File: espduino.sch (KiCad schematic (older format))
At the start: 14 parts, among them IC101 ATMEGA168-A, P101 CONN_01X12, P102 CONN_01X12, P103 FTDI, P104 CONN_01X02, SW101 SPST, X101 16Mhz

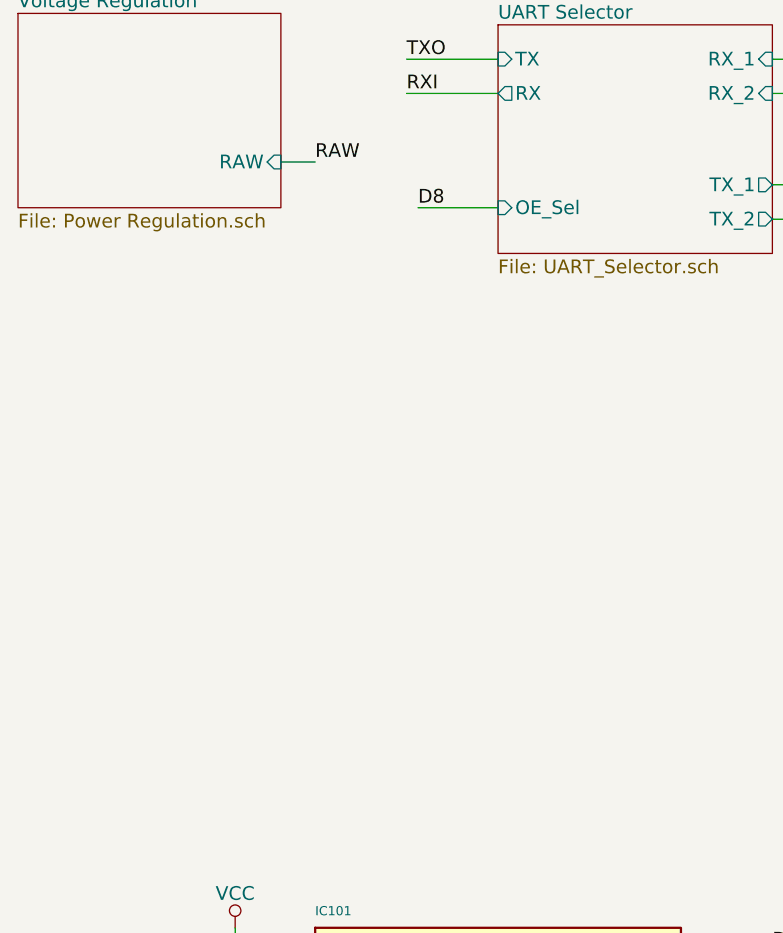
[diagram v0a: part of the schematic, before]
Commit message: Redesign the board and add USB
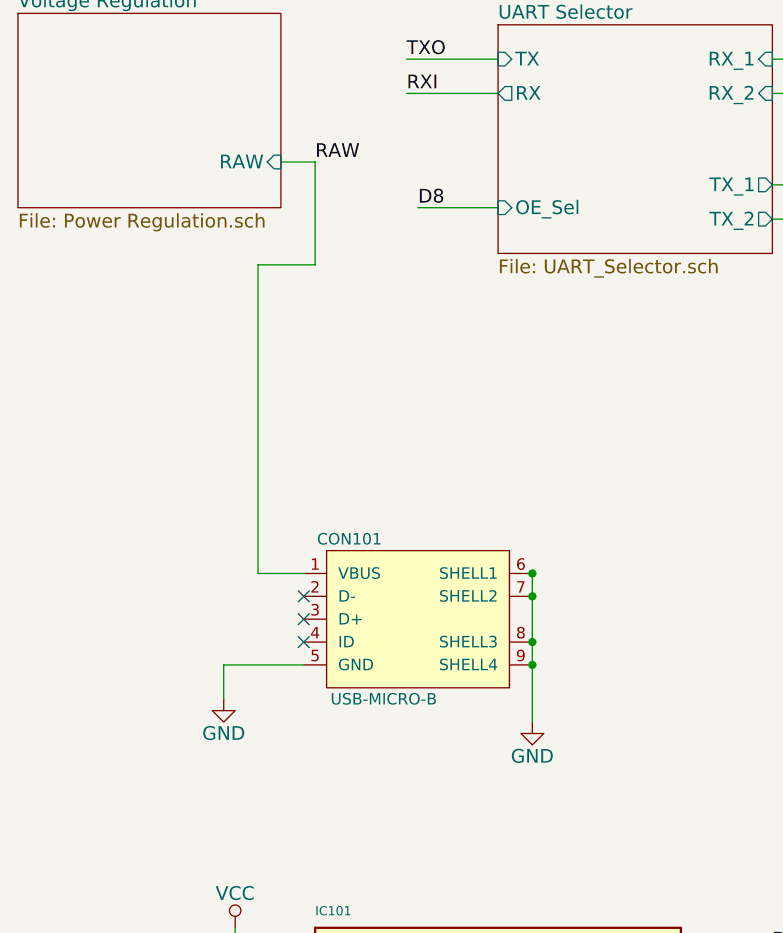
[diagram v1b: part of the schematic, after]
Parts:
- added CON101: USB-MICRO-B, symbol USB-MICRO-B
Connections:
- wire segments 91 -> 98
- no-connect marks 4 -> 7
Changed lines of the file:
@@
 Text Label 2300 850  0    60   ~ 0
 TXO
+$Comp
+L USB-MICRO-B CON101
+U 1 1 5538D1CF
+P 2350 3300
+F 0 "CON101" H 2050 3650 50  0000 C CNN
+F 1 "USB-MICRO-B" H 2200 2950 50  0000 C CNN
+F 2 "" H 2350 3200 50  0000 C CNN
+F 3 "" H 2350 3200 50  0000 C CNN
+	1    2350 3300
+	1    0    0    -1
+$EndComp
+Wire Wire Line
+	1850 3100 1650 3100
+Wire Wire Line
+	1650 3100 1650 1750
+Wire Wire Line
+	1650 1750 1900 1750
+Wire Wire Line
+	1900 1750 1900 1300
+$Comp
+L GND #PWR010
+U 1 1 5538D63B
+P 1500 3650
+F 0 "#PWR010" H 1500 3400 60  0001 C CNN
+F 1 "GND" H 1500 3500 60  0000 C CNN
+F 2 "" H 1500 3650 60  0000 C CNN
+F 3 "" H 1500 3650 60  0000 C CNN
+	1    1500 3650
+	1    0    0    -1
+$EndComp
+Wire Wire Line
+	1850 3500 1500 3500
+Wire Wire Line
+	1500 3500 1500 3650
+Wire Wire Line
+	2850 3100 2850 3750
+$Comp
+L GND #PWR011
+U 1 1 5538D7C0
+P 2850 3750
+F 0 "#PWR011" H 2850 3500 60  0001 C CNN
+F 1 "GND" H 2850 3600 60  0000 C CNN
+F 2 "" H 2850 3750 60  0000 C CNN
+F 3 "" H 2850 3750 60  0000 C CNN
+	1    2850 3750
+	1    0    0    -1
+$EndComp
+Connection ~ 2850 3500
+NoConn ~ 1850 3200
+NoConn ~ 1850 3300
+NoConn ~ 1850 3400
+Connection ~ 2850 3400
+Connection ~ 2850 3200
+Connection ~ 2850 3100
 $EndSCHEMATC

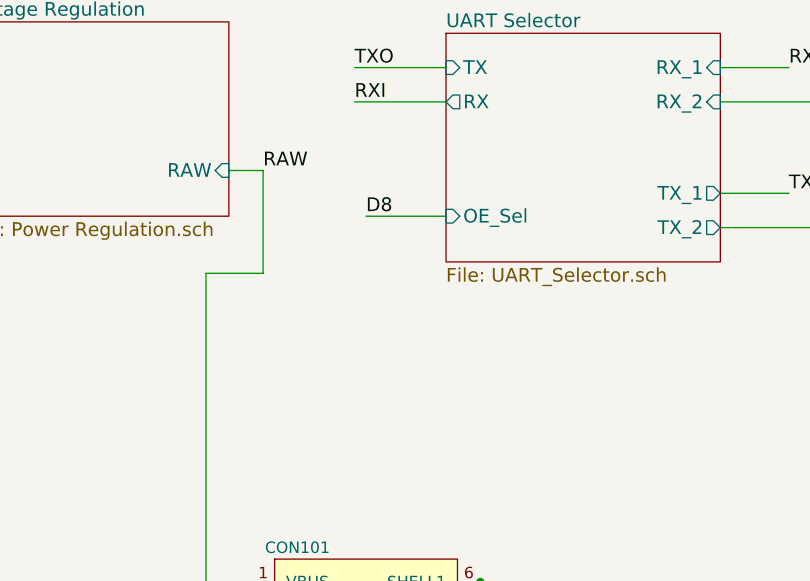
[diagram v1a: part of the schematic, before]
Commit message: Add mechanism to disable UART selector
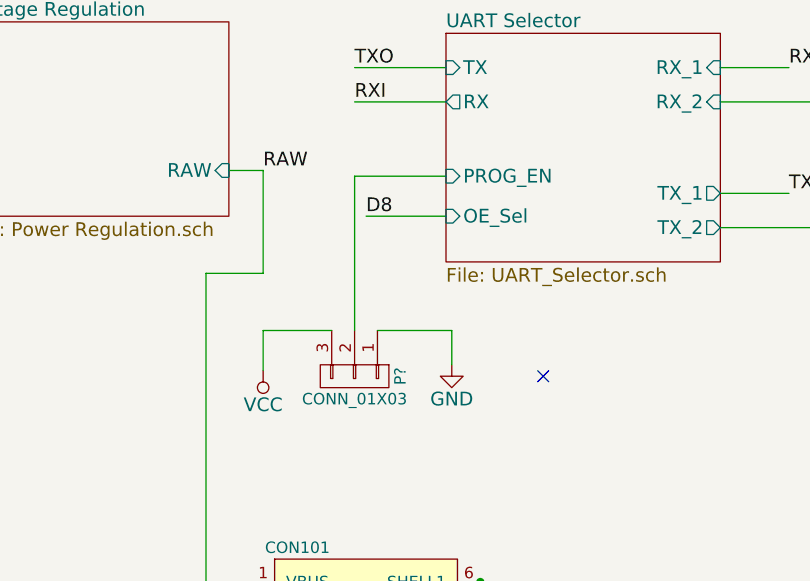
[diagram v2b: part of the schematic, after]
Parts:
- added P?: CONN_01X03, symbol CONN_01X03
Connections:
- wire segments 98 -> 104
- no-connect marks 7 -> 8
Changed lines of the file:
@@
 F7 "OE_Sel" I L 2700 1500 60
 F8 "RX" O L 2700 1000 60
+F9 "PROG_EN" I L 2700 1325 60
 $EndSheet
 Wire Wire Line
@@
 Connection ~ 2850 3200
 Connection ~ 2850 3100
+NoConn ~ 3125 2200
+Wire Wire Line
+	2300 1325 2700 1325
+$Comp
+L CONN_01X03 P?
+U 1 1 559105BB
+P 2300 2200
+F 0 "P?" H 2300 2400 50  0000 C CNN
+F 1 "CONN_01X03" V 2400 2200 50  0000 C CNN
+F 2 "" H 2300 2200 60  0000 C CNN
+F 3 "" H 2300 2200 60  0000 C CNN
+	1    2300 2200
+	0    1    1    0
+$EndComp
+Wire Wire Line
+	2300 2000 2300 1325
+$Comp
+L GND #PWR?
+U 1 1 559107D6
+P 2725 2150
+F 0 "#PWR?" H 2725 1900 60  0001 C CNN
+F 1 "GND" H 2725 2000 60  0000 C CNN
+F 2 "" H 2725 2150 60  0000 C CNN
+F 3 "" H 2725 2150 60  0000 C CNN
+	1    2725 2150
+	1    0    0    -1
+$EndComp
+$Comp
+L VCC #PWR?
+U 1 1 5591085F
+P 1900 2175
+F 0 "#PWR?" H 1900 2025 60  0001 C CNN
+F 1 "VCC" H 1900 2325 60  0000 C CNN
+F 2 "" H 1900 2175 60  0000 C CNN
+F 3 "" H 1900 2175 60  0000 C CNN
+	1    1900 2175
+	-1   0    0    1
+$EndComp
+Wire Wire Line
+	2725 2150 2725 2000
+Wire Wire Line
+	2725 2000 2400 2000
+Wire Wire Line
+	2200 2000 1900 2000
+Wire Wire Line
+	1900 2000 1900 2175
 $EndSCHEMATC

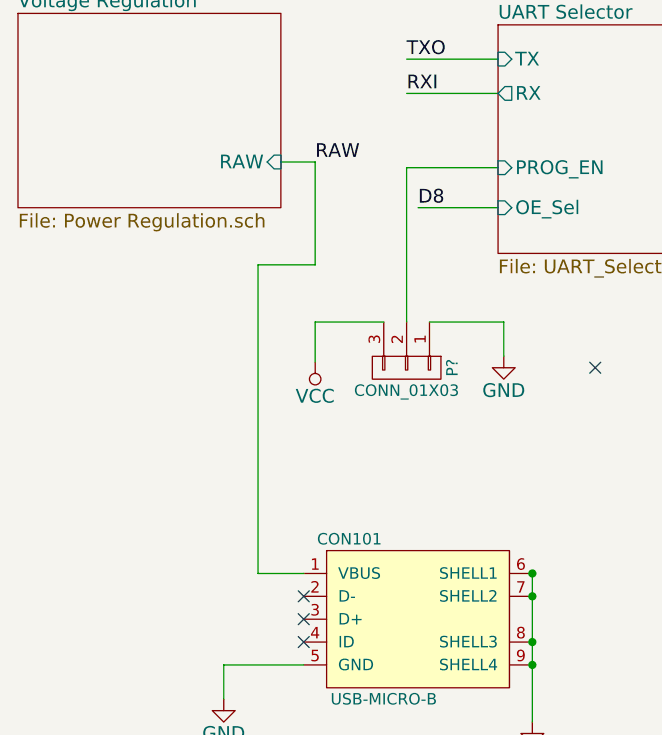
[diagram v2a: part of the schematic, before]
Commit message: Issue #4 RAW goes through LDO, +5v from USB doesn't
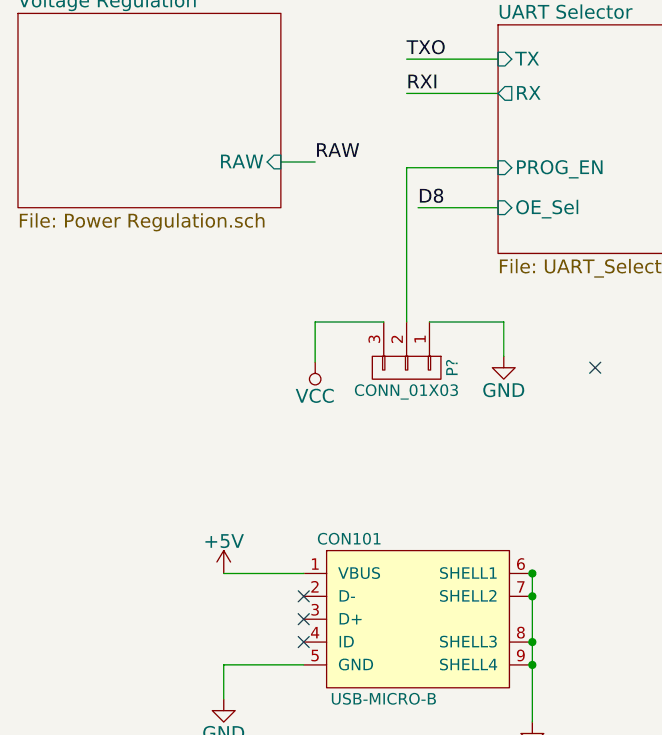
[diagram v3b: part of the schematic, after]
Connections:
- net labels added: +5V
- wire segments 104 -> 101
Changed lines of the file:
@@
 $EndComp
 Wire Wire Line
-	1850 3100 1650 3100
-Wire Wire Line
-	1650 3100 1650 1750
-Wire Wire Line
-	1650 1750 1900 1750
-Wire Wire Line
-	1900 1750 1900 1300
+	1500 3100 1850 3100
 $Comp
 L GND #PWR010
@@
 Wire Wire Line
 	1900 2000 1900 2175
+$Comp
+L +5V #PWR?
+U 1 1 55911357
+P 1500 3100
+F 0 "#PWR?" H 1500 2950 60  0001 C CNN
+F 1 "+5V" H 1500 3240 60  0000 C CNN
+F 2 "" H 1500 3100 60  0000 C CNN
+F 3 "" H 1500 3100 60  0000 C CNN
+	1    1500 3100
+	1    0    0    -1
+$EndComp
 $EndSCHEMATC

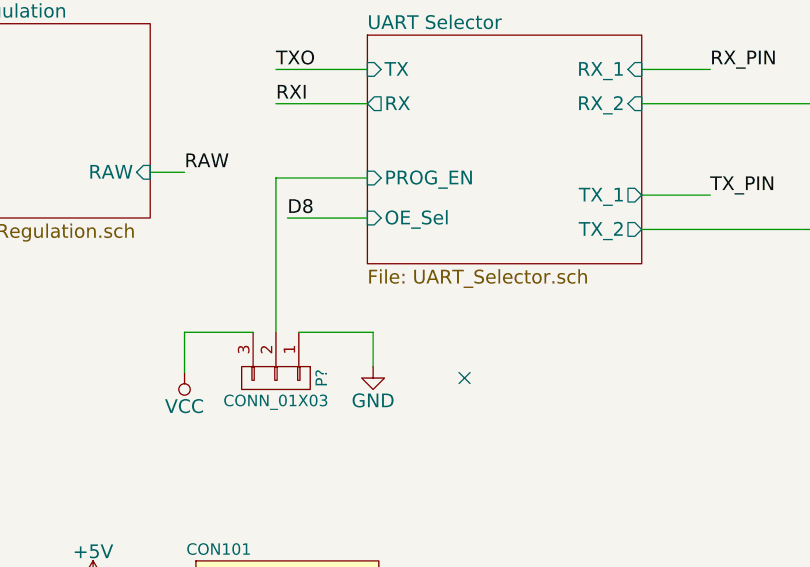
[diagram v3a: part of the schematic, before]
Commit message: Fix pin for ESP
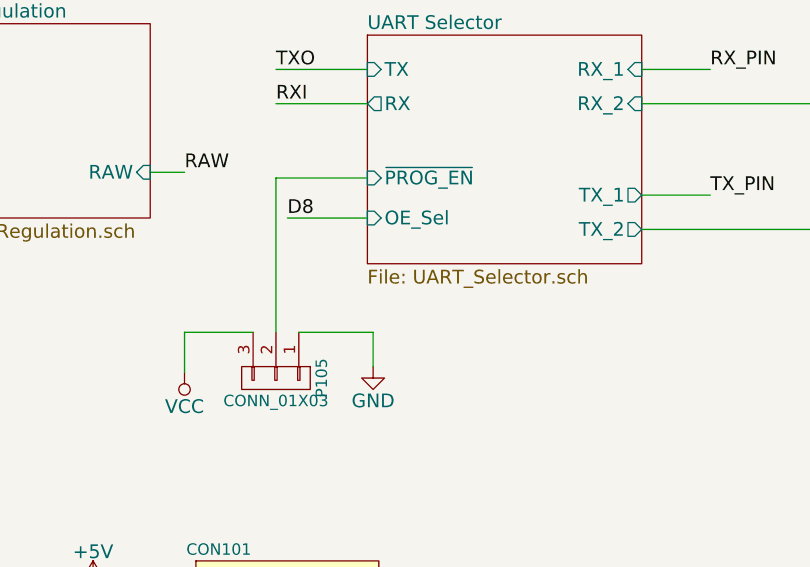
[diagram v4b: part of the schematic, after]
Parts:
- gave numbers to parts that had none: 1
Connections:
- no-connect marks 8 -> 7
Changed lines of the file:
@@
 F7 "OE_Sel" I L 2700 1500 60
 F8 "RX" O L 2700 1000 60
-F9 "PROG_EN" I L 2700 1325 60
+F9 "~PROG_EN" I L 2700 1325 60
 $EndSheet
 Wire Wire Line
@@
 Connection ~ 2850 3200
 Connection ~ 2850 3100
-NoConn ~ 3125 2200
 Wire Wire Line
 	2300 1325 2700 1325
 $Comp
-L CONN_01X03 P?
+L CONN_01X03 P105
 U 1 1 559105BB
 P 2300 2200
-F 0 "P?" H 2300 2400 50  0000 C CNN
+F 0 "P105" H 2300 2400 50  0000 C CNN
 F 1 "CONN_01X03" V 2400 2200 50  0000 C CNN
 F 2 "" H 2300 2200 60  0000 C CNN
@@
 	0    1    1    0
 $EndComp
-Wire Wire Line
-	2300 2000 2300 1325
 $Comp
-L GND #PWR?
+L GND #PWR012
 U 1 1 559107D6
 P 2725 2150
-F 0 "#PWR?" H 2725 1900 60  0001 C CNN
+F 0 "#PWR012" H 2725 1900 60  0001 C CNN
 F 1 "GND" H 2725 2000 60  0000 C CNN
 F 2 "" H 2725 2150 60  0000 C CNN
@@
 $EndComp
 $Comp
-L VCC #PWR?
+L VCC #PWR013
 U 1 1 5591085F
 P 1900 2175
-F 0 "#PWR?" H 1900 2025 60  0001 C CNN
+F 0 "#PWR013" H 1900 2025 60  0001 C CNN
 F 1 "VCC" H 1900 2325 60  0000 C CNN
 F 2 "" H 1900 2175 60  0000 C CNN
@@
 	1900 2000 1900 2175
 $Comp
-L +5V #PWR?
+L +5V #PWR014
 U 1 1 55911357
 P 1500 3100
-F 0 "#PWR?" H 1500 2950 60  0001 C CNN
+F 0 "#PWR014" H 1500 2950 60  0001 C CNN
 F 1 "+5V" H 1500 3240 60  0000 C CNN
 F 2 "" H 1500 3100 60  0000 C CNN
@@
 	1    0    0    -1
 $EndComp
+Wire Wire Line
+	2300 1325 2300 2000
 $EndSCHEMATC

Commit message: More fixes
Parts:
- removed IC101: ATMEGA168-A, LittlebushLogicFootPrints:TQFP32_08, symbol ATMEGA168-A
- added CON102: AVR-ISP-6, AVR-ISP-6, symbol AVR-ISP-6
- added IC101: ATMEGA328-P, TQFP32, symbol ATMEGA328-P
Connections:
- wire segments 101 -> 107
- no-connect marks 7 -> 8
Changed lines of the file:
@@
 $Descr A4 11693 8268
 encoding utf-8
-Sheet 1 4
+Sheet 1 5
 Title ""
 Date ""
@@
 $EndComp
 $Comp
-L VCC #PWR01
+L VCC #PWR104
 U 1 1 54F43D94
 P 1550 4650
-F 0 "#PWR01" H 1550 4500 60  0001 C CNN
+F 0 "#PWR104" H 1550 4500 60  0001 C CNN
 F 1 "VCC" H 1550 4800 60  0000 C CNN
 F 2 "" H 1550 4650 60  0000 C CNN
@@
 $EndComp
 $Comp
-L GND #PWR02
+L GND #PWR101
 U 1 1 54F43FD7
 P 1350 5750
-F 0 "#PWR02" H 1350 5500 60  0001 C CNN
+F 0 "#PWR101" H 1350 5500 60  0001 C CNN
 F 1 "GND" H 1350 5600 60  0000 C CNN
 F 2 "" H 1350 5750 60  0000 C CNN
@@
 $EndComp
 $Comp
-L GND #PWR03
+L GND #PWR105
 U 1 1 54F442ED
 P 1650 7050
-F 0 "#PWR03" H 1650 6800 60  0001 C CNN
+F 0 "#PWR105" H 1650 6800 60  0001 C CNN
 F 1 "GND" H 1650 6900 60  0000 C CNN
 F 2 "" H 1650 7050 60  0000 C CNN
@@
 Wire Wire Line
 	1550 5050 1750 5050
-Wire Wire Line
-	1750 4850 1550 4850
 Connection ~ 1550 4850
 Connection ~ 1550 4750
@@
 	1350 5350 1750 5350
 Wire Wire Line
-	1750 6850 1650 6850
-Wire Wire Line
-	1650 6850 1650 7050
-Wire Wire Line
 	1650 7050 1750 7050
 Wire Wire Line
 	1750 6950 1650 6950
-Connection ~ 1650 6950
 Wire Wire Line
 	3650 4750 3900 4750
@@
 Connection ~ 4700 5700
 $Comp
-L GND #PWR04
+L GND #PWR109
 U 1 1 54F456F6
 P 5350 5100
-F 0 "#PWR04" H 5350 4850 60  0001 C CNN
+F 0 "#PWR109" H 5350 4850 60  0001 C CNN
 F 1 "GND" H 5350 4950 60  0000 C CNN
 F 2 "" H 5350 5100 60  0000 C CNN
@@
 $EndComp
 $Comp
-L GND #PWR05
+L GND #PWR110
 U 1 1 54F45748
 P 5350 5700
-F 0 "#PWR05" H 5350 5450 60  0001 C CNN
+F 0 "#PWR110" H 5350 5450 60  0001 C CNN
 F 1 "GND" H 5350 5550 60  0000 C CNN
 F 2 "" H 5350 5700 60  0000 C CNN
@@
 	4500 6600 5000 6600
 $Comp
-L VCC #PWR06
+L VCC #PWR108
 U 1 1 54F46FC5
 P 4700 6100
-F 0 "#PWR06" H 4700 5950 60  0001 C CNN
+F 0 "#PWR108" H 4700 5950 60  0001 C CNN
 F 1 "VCC" H 4700 6250 60  0000 C CNN
 F 2 "" H 4700 6100 60  0000 C CNN
@@
 A5
 Connection ~ 5700 6800
-NoConn ~ 1750 6100
-NoConn ~ 1750 6200
-$Comp
-L GND #PWR07
+$Comp
+L GND #PWR112
 U 1 1 54F71020
 P 5950 6800
-F 0 "#PWR07" H 5950 6550 60  0001 C CNN
+F 0 "#PWR112" H 5950 6550 60  0001 C CNN
 F 1 "GND" H 5950 6650 60  0000 C CNN
 F 2 "" H 5950 6800 60  0000 C CNN
@@
 	5700 6800 5950 6800
 $Comp
-L GND #PWR08
+L GND #PWR111
 U 1 1 54F713D5
 P 5650 4800
-F 0 "#PWR08" H 5650 4550 60  0001 C CNN
+F 0 "#PWR111" H 5650 4550 60  0001 C CNN
 F 1 "GND" H 5650 4650 60  0000 C CNN
 F 2 "" H 5650 4800 60  0000 C CNN
@@
 $EndComp
 $Comp
-L PWR_FLAG #FLG09
+L PWR_FLAG #FLG101
 U 1 1 54F71E44
 P 5950 6800
-F 0 "#FLG09" H 5950 6895 30  0001 C CNN
+F 0 "#FLG101" H 5950 6895 30  0001 C CNN
 F 1 "PWR_FLAG" H 5950 6980 30  0000 C CNN
 F 2 "" H 5950 6800 60  0000 C CNN
 F 3 "" H 5950 6800 60  0000 C CNN
 	1    5950 6800
-	1    0    0    -1
-$EndComp
-$Comp
-L ATMEGA168-A IC101
-U 1 1 54EF0576
-P 2650 5850
-F 0 "IC101" H 1900 7100 40  0000 L BNN
-F 1 "ATMEGA168-A" H 3100 4450 40  0000 L BNN
-F 2 "LittlebushLogicFootPrints:TQFP32_08" H 2650 5850 30  0000 C CIN
-F 3 "" H 2650 5850 60  0000 C CNN
-	1    2650 5850
 	1    0    0    -1
 $EndComp
@@
 Text Label 2300 850  0    60   ~ 0
 TXO
-$Comp
-L USB-MICRO-B CON101
-U 1 1 5538D1CF
-P 2350 3300
-F 0 "CON101" H 2050 3650 50  0000 C CNN
-F 1 "USB-MICRO-B" H 2200 2950 50  0000 C CNN
-F 2 "" H 2350 3200 50  0000 C CNN
-F 3 "" H 2350 3200 50  0000 C CNN
-	1    2350 3300
-	1    0    0    -1
-$EndComp
 Wire Wire Line
 	1500 3100 1850 3100
 $Comp
-L GND #PWR010
+L GND #PWR103
 U 1 1 5538D63B
 P 1500 3650
-F 0 "#PWR010" H 1500 3400 60  0001 C CNN
+F 0 "#PWR103" H 1500 3400 60  0001 C CNN
 F 1 "GND" H 1500 3500 60  0000 C CNN
 F 2 "" H 1500 3650 60  0000 C CNN
@@
 Wire Wire Line
 	1500 3500 1500 3650
-Wire Wire Line
-	2850 3100 2850 3750
-$Comp
-L GND #PWR011
-U 1 1 5538D7C0
-P 2850 3750
-F 0 "#PWR011" H 2850 3500 60  0001 C CNN
-F 1 "GND" H 2850 3600 60  0000 C CNN
-F 2 "" H 2850 3750 60  0000 C CNN
-F 3 "" H 2850 3750 60  0000 C CNN
-	1    2850 3750
-	1    0    0    -1
-$EndComp
-Connection ~ 2850 3500
 NoConn ~ 1850 3200
 NoConn ~ 1850 3300
 NoConn ~ 1850 3400
-Connection ~ 2850 3400
-Connection ~ 2850 3200
-Connection ~ 2850 3100
 Wire Wire Line
 	2300 1325 2700 1325
@@
 $EndComp
 $Comp
-L GND #PWR012
+L GND #PWR107
 U 1 1 559107D6
 P 2725 2150
-F 0 "#PWR012" H 2725 1900 60  0001 C CNN
+F 0 "#PWR107" H 2725 1900 60  0001 C CNN
 F 1 "GND" H 2725 2000 60  0000 C CNN
 F 2 "" H 2725 2150 60  0000 C CNN
@@
 $EndComp
 $Comp
-L VCC #PWR013
+L VCC #PWR106
 U 1 1 5591085F
 P 1900 2175
-F 0 "#PWR013" H 1900 2025 60  0001 C CNN
+F 0 "#PWR106" H 1900 2025 60  0001 C CNN
 F 1 "VCC" H 1900 2325 60  0000 C CNN
 F 2 "" H 1900 2175 60  0000 C CNN
@@
 	1900 2000 1900 2175
 $Comp
-L +5V #PWR014
+L +5V #PWR102
 U 1 1 55911357
 P 1500 3100
-F 0 "#PWR014" H 1500 2950 60  0001 C CNN
+F 0 "#PWR102" H 1500 2950 60  0001 C CNN
 F 1 "+5V" H 1500 3240 60  0000 C CNN
 F 2 "" H 1500 3100 60  0000 C CNN
@@
 Wire Wire Line
 	2300 1325 2300 2000
+$Comp
+L USB-MICRO-B CON101
+U 1 1 5538D1CF
+P 2350 3300
+F 0 "CON101" H 2050 3650 50  0000 C CNN
+F 1 "USB-MICRO-B" H 2200 2950 50  0000 C CNN
+F 2 "" H 2350 3200 50  0000 C CNN
+F 3 "" H 2350 3200 50  0000 C CNN
+	1    2350 3300
+	1    0    0    -1
+$EndComp
+NoConn ~ 2850 3500
+NoConn ~ 2850 3400
+NoConn ~ 2850 3200
+Wire Wire Line
+	1500 3650 3025 3650
+Wire Wire Line
+	3025 3650 3025 3100
+Wire Wire Line
+	3025 3100 2850 3100
+$Comp
+L ATMEGA328-P IC101
+U 1 1 5593AEC4
+P 2650 5850
+F 0 "IC101" H 1900 7100 40  0000 L BNN
+F 1 "ATMEGA328-P" H 3050 4450 40  0000 L BNN
+F 2 "TQFP32" H 2650 5850 30  0000 C CIN
+F 3 "" H 2650 5850 60  0000 C CNN
+	1    2650 5850
+	1    0    0    -1
+$EndComp
+Wire Wire Line
+	1650 6950 1650 7050
+$Sheet
+S 9725 1100 825  550
+U 559CE2A1
+F0 "Freezy" 60
+F1 "Freezy.sch" 60
+$EndSheet
+$Comp
+L AVR-ISP-6 CON102
+U 1 1 559DF1DC
+P 7575 4500
+F 0 "CON102" H 7495 4740 50  0000 C CNN
+F 1 "AVR-ISP-6" H 7335 4270 50  0000 L BNN
+F 2 "AVR-ISP-6" V 7055 4540 50  0001 C CNN
+F 3 "" H 7575 4500 60  0000 C CNN
+	1    7575 4500
+	1    0    0    -1
+$EndComp
+Wire Wire Line
+	7700 4400 8100 4400
+Wire Wire Line
+	7700 4500 8100 4500
+Wire Wire Line
+	7700 4600 8100 4600
+Wire Wire Line
+	7450 4400 7000 4400
+Wire Wire Line
+	7450 4500 7000 4500
+Wire Wire Line
+	7450 4600 7000 4600
+Text Label 8100 4400 0    60   ~ 0
+VCC
+Text Label 8100 4500 0    60   ~ 0
+MOSI
+Text Label 8100 4600 0    60   ~ 0
+GND
+Text Label 7000 4400 2    60   ~ 0
+MISO
+Text Label 7000 4500 2    60   ~ 0
+SCK
+Text Label 7000 4600 2    60   ~ 0
+RESET
 $EndSCHEMATC
